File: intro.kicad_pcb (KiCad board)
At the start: 2 copper layers, 148.5 x 110.1 mm, 122 parts, among them IC1 IS31FL3741A-QFLS4-TR, SW1 SW_Push, SW10 SW_Push, SW11 SW_Push, SW12 SW_Push, SW13 SW_Push, SW14 SW_Push, SW15 SW_Push, SW16 SW_Push, SW17 SW_Push, SW18 SW_Push, SW19 SW_Push, SW2 SW_Push, SW20 SW_Push, SW21 SW_Push, SW22 SW_Push, SW23 SW_Push, SW24 SW_Push, SW25 SW_Push, SW26 SW_Push, SW27 SW_Push, SW28 SW_Push, SW29 SW_Push, SW3 SW_Push, SW30 SW_Push, SW31 SW_Push, SW32 SW_Push, SW33 SW_Push, SW34 SW_Push, SW35 RotaryEncoder_Switch, SW4 SW_Push, SW5 SW_Push, SW6 SW_Push, SW7 SW_Push, SW8 SW_Push, SW9 SW_Push, U1 nice_nano

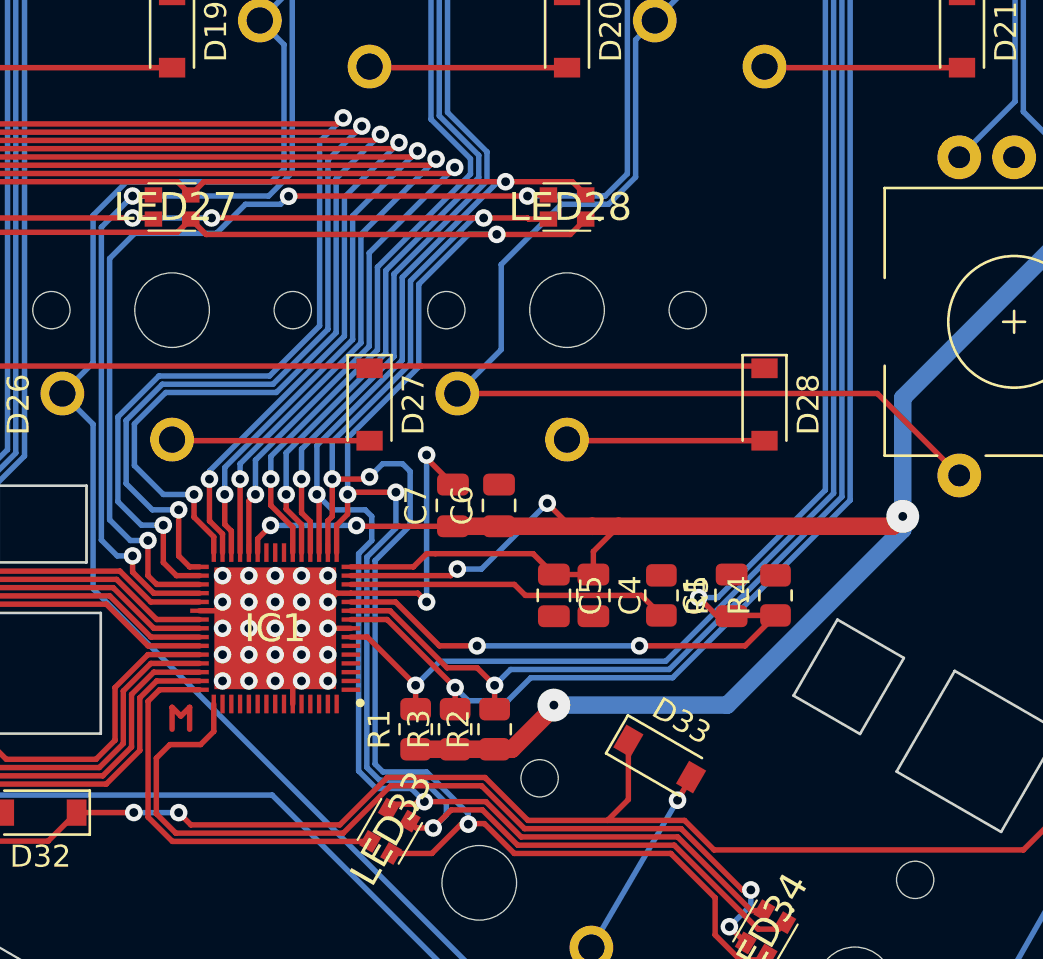
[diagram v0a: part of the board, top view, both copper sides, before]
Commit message: Begin improving bypass caps
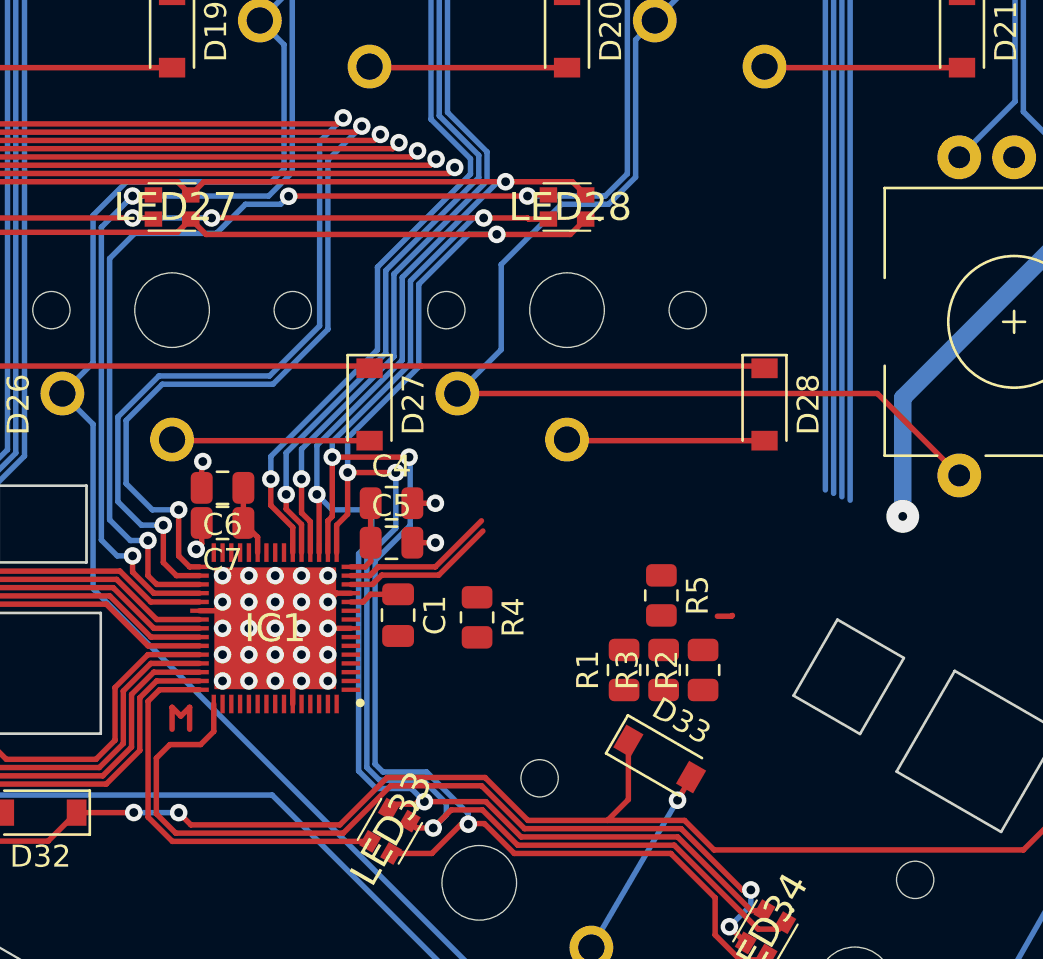
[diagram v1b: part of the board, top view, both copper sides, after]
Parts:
- moved C1 15.2 mm to (181.8, 108.9), turned to -90 degrees
- moved R4 13.6 mm to (185.4, 109.0), turned to -90 degrees
- moved C6 12.6 mm to (173.8, 103.1), turned to 180 degrees
- moved C7 10.5 mm to (173.8, 104.7), turned to 180 degrees
- moved C4 10.1 mm to (181.5, 103.8), turned to 0 degrees
- moved R1 9.88 mm to (192.1, 111.4)
- moved R2 9.88 mm to (195.7, 111.4)
- moved R3 9.88 mm to (193.9, 111.4)
- moved C5 7.78 mm to (181.5, 105.6), turned to 0 degrees
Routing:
- net VCC: track 146.7 -> 75.9 mm, vias 6 -> 1
- net SDB: track 92.3 -> 62.2 mm, vias 5 -> 2
- net SDA: track 75.2 -> 46.2 mm, vias 2 -> 1
- net CS5: track 111.1 -> 82.1 mm, vias 5 -> 4
- net SCL: track 72.4 -> 44.0 mm, vias 2 -> 1
- net INTB: track 64.3 -> 36.6 mm, vias 1 -> 0
- net CS4: track 124.0 -> 101.5 mm, vias 5 -> 4
- net CS3: track 142.8 -> 120.7 mm, vias 5 -> 4
- net CS2: track 161.5 -> 139.9 mm, vias 5 -> 4
- net CS1: track 185.1 -> 163.7 mm, vias 5 -> 4
- net Net-(IC1-Pad13): track 14.7 -> 7.02 mm
- net GND: track 24.4 -> 17.6 mm, vias 27 -> 29
- net RSW3: track 389.6 -> 390.5 mm

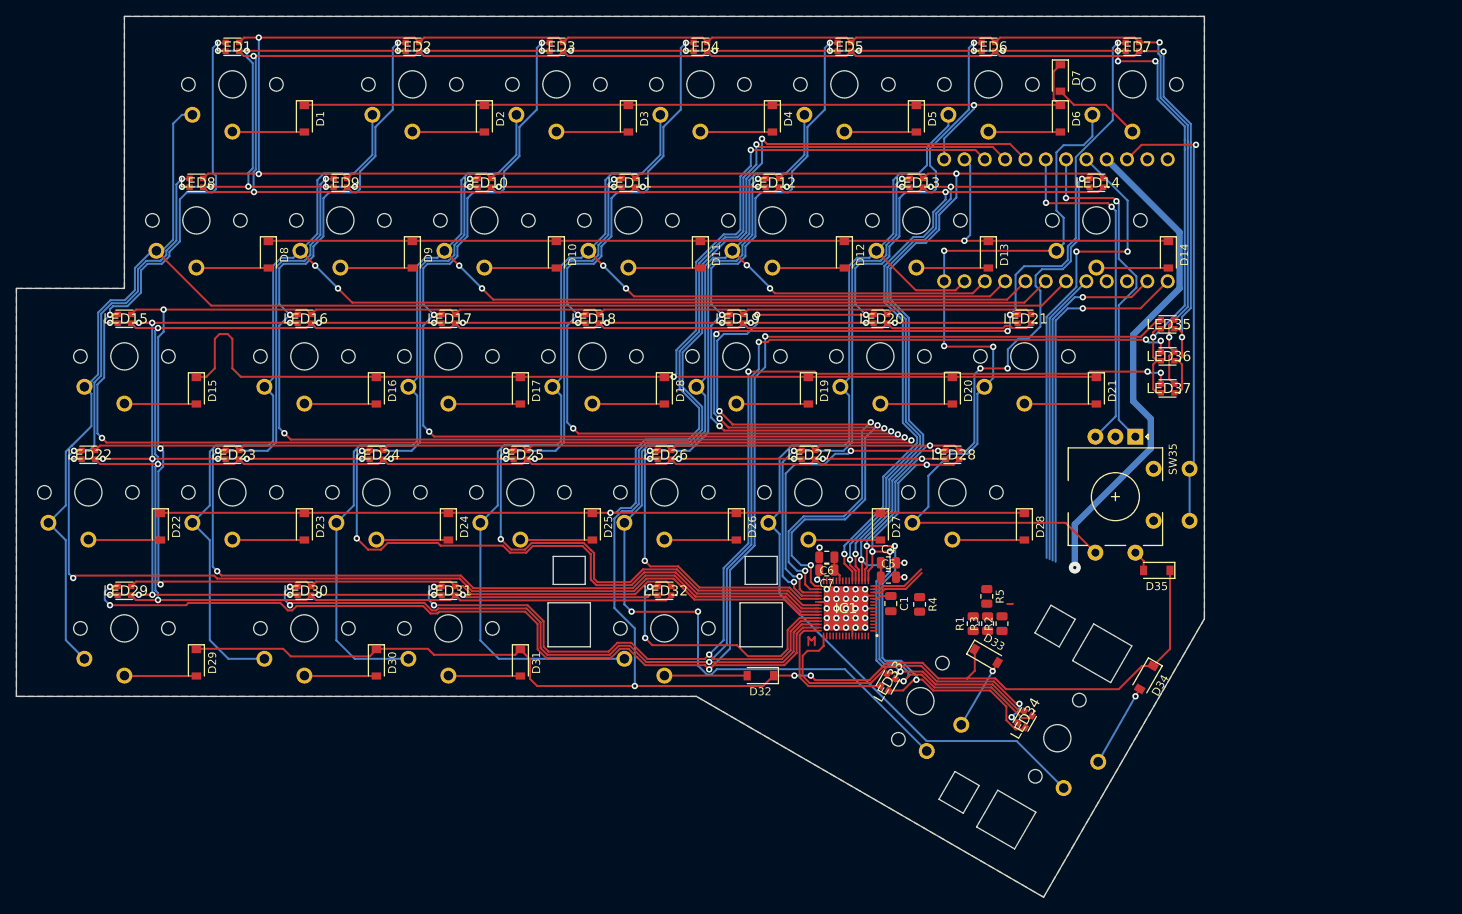
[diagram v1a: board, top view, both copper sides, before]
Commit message: Set up LED routing
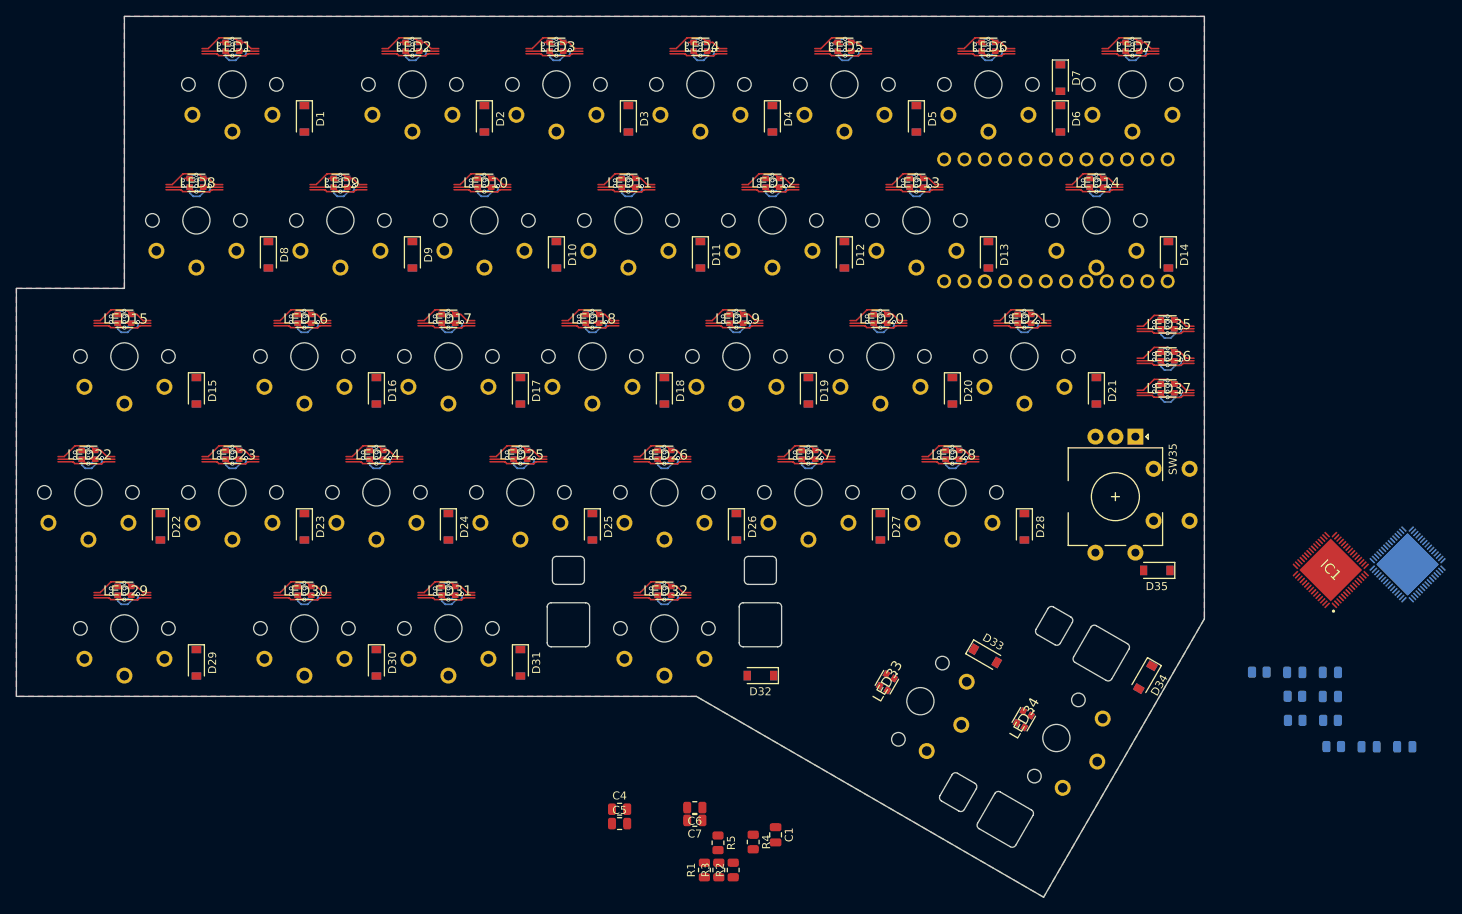
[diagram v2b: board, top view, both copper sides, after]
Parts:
- removed S1, S2: Choc_stab, intro:Kailh-PG1350-2u-STAB
- added C10: 0.1μF, Capacitor_SMD:C_0805_2012Metric, B.Cu at (236.7, 120.5)
- added C2: 0.1μF, Capacitor_SMD:C_0805_2012Metric, B.Cu at (232.3, 117.5)
- added C3: 1μF, Capacitor_SMD:C_0805_2012Metric, B.Cu at (241.6, 126.8)
- added C8: 0.1μF, Capacitor_SMD:C_0805_2012Metric, B.Cu at (236.7, 117.5)
- added C9: 1μF, Capacitor_SMD:C_0805_2012Metric, B.Cu at (246.0, 126.8)
- added IC2: IS31FL3741A-QFLS4-TR, intro:QFN40P700X700X80-61N-D, B.Cu at (246.4, 104.0)
- added R10: 10kΩ, Resistor_SMD:R_0805_2012Metric, B.Cu at (237.2, 126.8)
- added R6: 100kΩ, Resistor_SMD:R_0805_2012Metric, B.Cu at (227.9, 117.5)
- added R7: 2kΩ, Resistor_SMD:R_0805_2012Metric, B.Cu at (232.4, 123.5)
- added R8: 2kΩ, Resistor_SMD:R_0805_2012Metric, B.Cu at (236.8, 123.5)
- added R9: 100kΩ, Resistor_SMD:R_0805_2012Metric, B.Cu at (232.3, 120.5)
- D1, D10, D11, D12, D13, D14, D15, D16, D17, D18, D19, D2, D20, D21, D22, D23, D24, D25, D26, D27, D28, D29, D3, D30, D31, D32, D33, D34, D35, D4, D5, D6, D7, D8, D9: footprint Diode_SMD:D_SOD-123 -> intro:D_SOD-123_Reversible
- LED1, LED10, LED11, LED12, LED13, LED14, LED15, LED16, LED17, LED18, LED19, LED2, LED20, LED21, LED22, LED23, LED24, LED25, LED26, LED27, LED28, LED29, LED3, LED30, LED31, LED32, LED33, LED34, LED35, LED36, LED37, LED4, LED5, LED6, LED7, LED8, LED9: footprint intro:FMB2020RGBAHG -> intro:FMB2020RGBAHG_Reversible
- SW1, SW14, SW15, SW29, SW33: footprint intro:SW_choc_1.5u -> intro:SW_choc_Reversible_1.5u
- SW10, SW11, SW12, SW13, SW16, SW17, SW18, SW19, SW2, SW20, SW21, SW22, SW23, SW24, SW25, SW26, SW27, SW28, SW3, SW30, SW31, SW4, SW5, SW6, SW7, SW8, SW9: footprint intro:SW_choc_1u -> intro:SW_choc_Reversible_1u
- SW32, SW34: footprint intro:SW_choc_1u -> intro:SW_choc_Reversible_2u_STAB
- moved IC1 60.8 mm to (236.8, 104.7), turned to 135 degrees
- moved R5 45.6 mm to (160.2, 138.8)
- moved C5 45.6 mm to (147.9, 136.4)
- moved C4 45.6 mm to (147.9, 134.6)
- moved R1 45.6 mm to (158.5, 142.2)
- moved R2 45.6 mm to (162.1, 142.2)
- moved R3 45.6 mm to (160.3, 142.2)
- moved R4 36.3 mm to (164.6, 138.7)
- moved C6 35.4 mm to (157.3, 134.4)
- moved C7 35.4 mm to (157.3, 136.0)
- moved C1 32.3 mm to (167.4, 137.8)
- moved D34 0.12 mm to (213.6, 118.1)
- moved LED34 0.12 mm to (198.4, 123.3)
- moved SW34 0.12 mm to (202.5, 125.7)
- moved D33 0.12 mm to (193.6, 115.4)
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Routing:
- net row4: track 263.3 -> 0.00 mm, vias 4 -> 0
- net RSW1: track 403.4 -> 172.9 mm, vias 37 -> 18
- net RSW2: track 390.5 -> 166.6 mm, vias 6 -> 18
- net RSW4: track 368.8 -> 163.3 mm, vias 31 -> 17
- net RSW5: track 359.6 -> 157.3 mm, vias 6 -> 17
- net row3: track 201.2 -> 0.00 mm, vias 2 -> 0
- net col0: track 198.9 -> 0.00 mm
- net CS15: track 197.8 -> 5.72 mm
- net col1: track 188.5 -> 0.00 mm, vias 2 -> 0
- net row2: track 184.7 -> 0.00 mm, vias 2 -> 0
- net RSW3: track 390.5 -> 213.2 mm, vias 7 -> 54
- net col2: track 168.9 -> 0.00 mm, vias 2 -> 0
- net CS16: track 174.0 -> 5.72 mm, vias 6 -> 4
- net col4: track 162.0 -> 0.00 mm, vias 4 -> 0
- net CS1: track 163.7 -> 5.72 mm
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
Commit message: Wiring switches & diodes
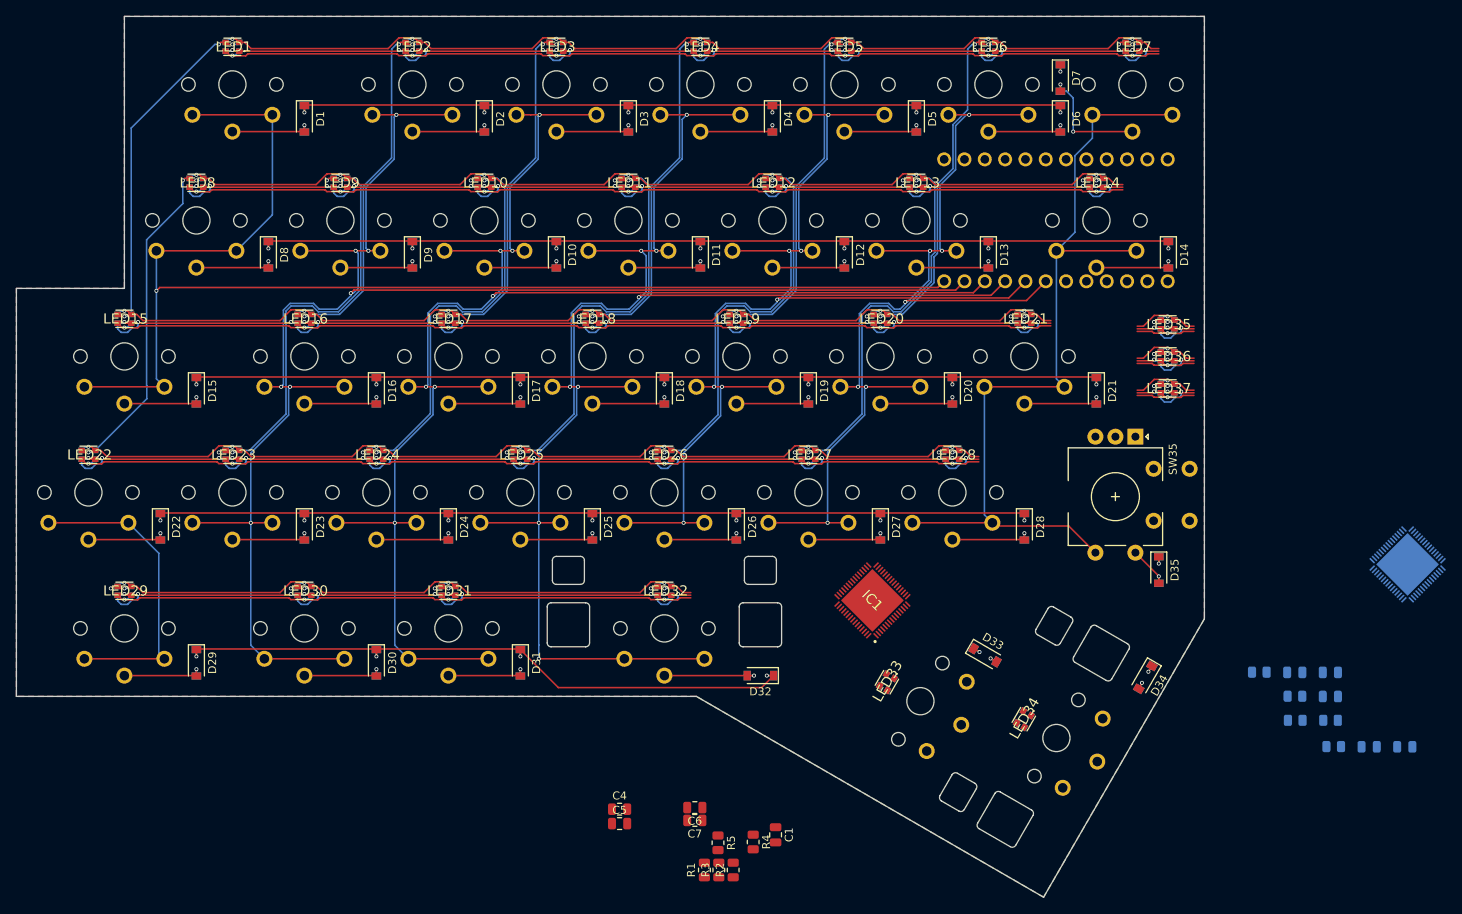
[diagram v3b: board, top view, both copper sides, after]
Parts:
- moved IC1 57.4 mm to (179.5, 108.5)
- moved D35 0.25 mm to (215.3, 104.7), turned to -90 degrees
- moved D33 0.08 mm to (193.6, 115.4)
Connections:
- U1 pad 10: col4 -> col2
- U1 pad 11: col5 -> col1
- U1 pad 12: SW35A -> col0
- U1 pad 6: col0 -> SW35A
- U1 pad 7: col1 -> col5
- U1 pad 8: col2 -> col4
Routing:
- net col1: track 0.00 -> 208.5 mm, vias 0 -> 7
- net col0: track 0.00 -> 204.1 mm, vias 0 -> 1
- net col2: track 0.00 -> 193.1 mm, vias 0 -> 7
- net col3: track 0.00 -> 188.1 mm, vias 0 -> 8
- net RSW3: track 213.2 -> 385.1 mm, vias 54 -> 51
- net RSW1: track 172.9 -> 342.7 mm
- net RSW2: track 166.6 -> 334.9 mm
- net col4: track 0.00 -> 135.2 mm, vias 0 -> 7
- net RSW4: track 163.3 -> 295.3 mm
- net RSW5: track 157.3 -> 288.3 mm
- net RSW6: track 201.3 -> 330.4 mm, vias 51 -> 48
- net row1: track 0.00 -> 124.8 mm, vias 0 -> 7
- net row2: track 0.00 -> 124.8 mm, vias 0 -> 7
- net col5: track 0.00 -> 120.5 mm, vias 0 -> 7
- net row3: track 0.00 -> 120.3 mm, vias 0 -> 7
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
